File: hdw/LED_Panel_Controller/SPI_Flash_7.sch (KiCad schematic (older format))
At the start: 14 parts, among them U3101 74LVC1G97, U3102 SST25VF080B-50-4I-S2AF

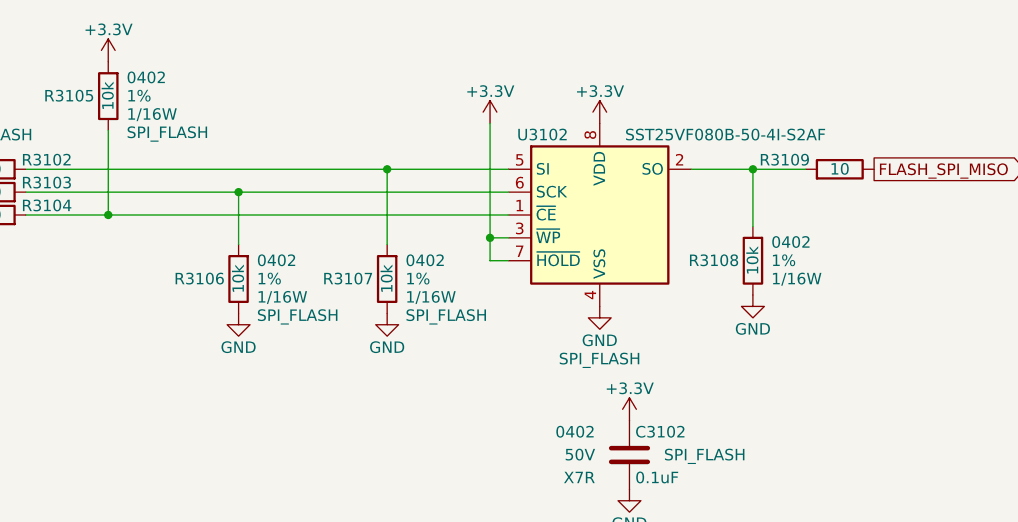
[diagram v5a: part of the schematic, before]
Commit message: fixed SPI flash pull resistors, more PCB placement
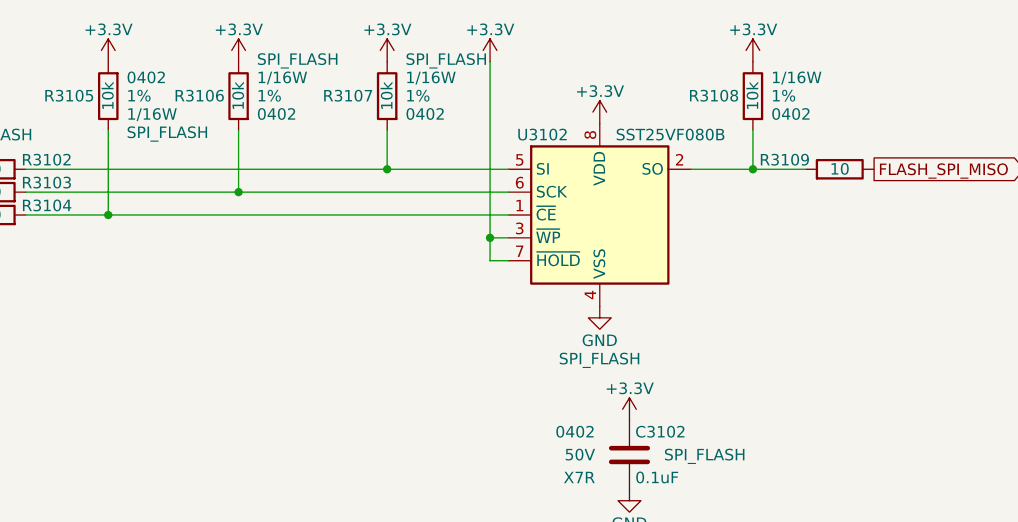
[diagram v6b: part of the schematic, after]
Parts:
- U3102: value SST25VF080B-50-4I-S2AF -> SST25VF080B
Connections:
- net +3V3: now also R3106.2, R3107.2, R3108.2
- net GND: no longer R3106.2, R3107.2, R3108.2
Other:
- moved on the sheet: R3106, R3107, R3108
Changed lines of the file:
@@
 L Custom_Library:R_Custom R3108
 U 1 1 60786265
-P 6750 3850
-F 0 "R3108" H 6690 3850 50  0000 R CNN
-F 1 "10k" V 6750 3850 50  0000 C CNN
-F 2 "Resistors_SMD:R_0402" H 6750 3850 50  0001 C CNN
-F 3 "" H 6750 3850 50  0001 C CNN
-F 4 "0402" H 6830 3930 50  0000 L CNN "display_footprint"
-F 5 "1%" H 6830 3850 50  0000 L CNN "Tolerance"
-F 6 "1/16W" H 6830 3770 50  0000 L CNN "Wattage"
-F 7 "RMCF0402FT10K0CT-ND" H 7050 4250 60  0001 C CNN "Digi-Key PN"
-	1    6750 3850
-	1    0    0    -1
-$EndComp
-$Comp
-L power:GND #PWR03108
-U 1 1 6078626D
-P 5150 4080
-F 0 "#PWR03108" H 5150 3830 50  0001 C CNN
-F 1 "GND" H 5150 3930 50  0000 C CNN
-F 2 "" H 5150 4080 50  0001 C CNN
-F 3 "" H 5150 4080 50  0001 C CNN
-	1    5150 4080
-	1    0    0    -1
-$EndComp
-$Comp
-L power:GND #PWR03114
-U 1 1 60786277
-P 6750 4000
-F 0 "#PWR03114" H 6750 3750 50  0001 C CNN
-F 1 "GND" H 6750 3850 50  0000 C CNN
-F 2 "" H 6750 4000 50  0001 C CNN
-F 3 "" H 6750 4000 50  0001 C CNN
-	1    6750 4000
-	1    0    0    -1
+P 6750 3130
+F 0 "R3108" H 6690 3130 50  0000 R CNN
+F 1 "10k" V 6750 3130 50  0000 C CNN
+F 2 "Resistors_SMD:R_0402" H 6750 3130 50  0001 C CNN
+F 3 "" H 6750 3130 50  0001 C CNN
+F 4 "0402" H 6830 3210 50  0000 L CNN "display_footprint"
+F 5 "1%" H 6830 3130 50  0000 L CNN "Tolerance"
+F 6 "1/16W" H 6830 3050 50  0000 L CNN "Wattage"
+F 7 "RMCF0402FT10K0CT-ND" H 7050 3530 60  0001 C CNN "Digi-Key PN"
+	1    6750 3130
+	1    0    0    1
 $EndComp
 $Comp
@@
 $EndComp
 Wire Wire Line
-	5150 3450 5150 3780
-Connection ~ 5150 3450
-Wire Wire Line
-	5150 3450 5680 3450
-Wire Wire Line
 	3930 3280 3930 3650
 Wire Wire Line
 	3930 3650 5680 3650
 Connection ~ 3930 3650
-Wire Wire Line
-	6980 3450 6750 3450
-Wire Wire Line
-	6750 3700 6750 3450
-Connection ~ 6750 3450
-Wire Wire Line
-	6750 3450 6480 3450
 Text GLabel 7280 3450 2    50   Output ~ 0
 FLASH_SPI_MISO
@@
 P 6080 3650
 F 0 "U3102" H 5830 4000 50  0000 C CNN
-F 1 "SST25VF080B-50-4I-S2AF" H 6630 4000 50  0000 C CNN
+F 1 "SST25VF080B" H 6630 4000 50  0000 R CNN
 F 2 "Package_SO:SOIC-8_5.275x5.275mm_P1.27mm" H 6080 2950 50  0001 C CNN
 F 3 "http://ww1.microchip.com/downloads/en/DeviceDoc/20005045C.pdf" H 6030 4200 50  0001 C CNN
@@
 L power:+3.3V #PWR03109
 U 1 1 6078630E
-P 5600 3250
-F 0 "#PWR03109" H 5600 3100 50  0001 C CNN
-F 1 "+3.3V" H 5600 3390 50  0000 C CNN
-F 2 "" H 5600 3250 50  0001 C CNN
-F 3 "" H 5600 3250 50  0001 C CNN
-	1    5600 3250
+P 5600 2980
+F 0 "#PWR03109" H 5600 2830 50  0001 C CNN
+F 1 "+3.3V" H 5600 3120 50  0000 C CNN
+F 2 "" H 5600 2980 50  0001 C CNN
+F 3 "" H 5600 2980 50  0001 C CNN
+	1    5600 2980
 	1    0    0    -1
 $EndComp
@@
 	5680 3750 5600 3750
 Wire Wire Line
-	5600 3750 5600 3250
+	5600 3750 5600 2980
 Wire Wire Line
 	5680 3850 5600 3850
@@
 	5600 3850 5600 3750
 Connection ~ 5600 3750
-Wire Wire Line
-	3570 3550 4500 3550
 $Comp
 L Custom_Library:R_Custom R3106
 U 1 1 60786315
-P 4500 3930
-F 0 "R3106" H 4440 3930 50  0000 R CNN
-F 1 "10k" V 4500 3930 50  0000 C CNN
-F 2 "Resistors_SMD:R_0402" H 4500 3930 50  0001 C CNN
-F 3 "" H 4500 3930 50  0001 C CNN
-F 4 "0402" H 4580 4010 50  0000 L CNN "display_footprint"
-F 5 "1%" H 4580 3930 50  0000 L CNN "Tolerance"
-F 6 "1/16W" H 4580 3850 50  0000 L CNN "Wattage"
-F 7 "RMCF0402FT10K0CT-ND" H 4800 4330 60  0001 C CNN "Digi-Key PN"
-F 8 "SPI_FLASH" H 4580 3770 50  0000 L CNN "Configuration"
-	1    4500 3930
-	1    0    0    -1
-$EndComp
-$Comp
-L power:GND #PWR03107
-U 1 1 6078631A
-P 4500 4080
-F 0 "#PWR03107" H 4500 3830 50  0001 C CNN
-F 1 "GND" H 4500 3930 50  0000 C CNN
-F 2 "" H 4500 4080 50  0001 C CNN
-F 3 "" H 4500 4080 50  0001 C CNN
-	1    4500 4080
-	1    0    0    -1
-$EndComp
-Wire Wire Line
-	3570 3450 5150 3450
-Wire Wire Line
-	4500 3550 4500 3780
-Connection ~ 4500 3550
-Wire Wire Line
-	4500 3550 5680 3550
+P 4500 3130
+F 0 "R3106" H 4440 3130 50  0000 R CNN
+F 1 "10k" V 4500 3130 50  0000 C CNN
+F 2 "Resistors_SMD:R_0402" H 4500 3130 50  0001 C CNN
+F 3 "" H 4500 3130 50  0001 C CNN
+F 4 "0402" H 4580 3210 50  0000 L CNN "display_footprint"
+F 5 "1%" H 4580 3130 50  0000 L CNN "Tolerance"
+F 6 "1/16W" H 4580 3050 50  0000 L CNN "Wattage"
+F 7 "RMCF0402FT10K0CT-ND" H 4800 3530 60  0001 C CNN "Digi-Key PN"
+F 8 "SPI_FLASH" H 4580 2970 50  0000 L CNN "Configuration"
+	1    4500 3130
+	1    0    0    1
+$EndComp
 $Comp
 L Custom_Library:R_Custom R3103
@@
 L Custom_Library:R_Custom R3107
 U 1 1 60786357
-P 5150 3930
-F 0 "R3107" H 5090 3930 50  0000 R CNN
-F 1 "10k" V 5150 3930 50  0000 C CNN
-F 2 "Resistors_SMD:R_0402" H 5150 3930 50  0001 C CNN
-F 3 "" H 5150 3930 50  0001 C CNN
-F 4 "0402" H 5230 4010 50  0000 L CNN "display_footprint"
-F 5 "1%" H 5230 3930 50  0000 L CNN "Tolerance"
-F 6 "1/16W" H 5230 3850 50  0000 L CNN "Wattage"
-F 7 "RMCF0402FT10K0CT-ND" H 5450 4330 60  0001 C CNN "Digi-Key PN"
-F 8 "SPI_FLASH" H 5230 3770 50  0000 L CNN "Configuration"
-	1    5150 3930
-	1    0    0    -1
+P 5150 3130
+F 0 "R3107" H 5090 3130 50  0000 R CNN
+F 1 "10k" V 5150 3130 50  0000 C CNN
+F 2 "Resistors_SMD:R_0402" H 5150 3130 50  0001 C CNN
+F 3 "" H 5150 3130 50  0001 C CNN
+F 4 "0402" H 5230 3210 50  0000 L CNN "display_footprint"
+F 5 "1%" H 5230 3130 50  0000 L CNN "Tolerance"
+F 6 "1/16W" H 5230 3050 50  0000 L CNN "Wattage"
+F 7 "RMCF0402FT10K0CT-ND" H 5450 3530 60  0001 C CNN "Digi-Key PN"
+F 8 "SPI_FLASH" H 5230 2970 50  0000 L CNN "Configuration"
+	1    5150 3130
+	1    0    0    1
 $EndComp
 $Comp
@@
 	1    0    0    -1
 $EndComp
+Wire Wire Line
+	3570 3450 5150 3450
+Wire Wire Line
+	3570 3550 4500 3550
+$Comp
+L power:+3.3V #PWR0124
+U 1 1 606A1000
+P 5150 2980
+F 0 "#PWR0124" H 5150 2830 50  0001 C CNN
+F 1 "+3.3V" H 5150 3120 50  0000 C CNN
+F 2 "" H 5150 2980 50  0001 C CNN
+F 3 "" H 5150 2980 50  0001 C CNN
+	1    5150 2980
+	1    0    0    -1
+$EndComp
+$Comp
+L power:+3.3V #PWR0125
+U 1 1 606A13DE
+P 4500 2980
+F 0 "#PWR0125" H 4500 2830 50  0001 C CNN
+F 1 "+3.3V" H 4500 3120 50  0000 C CNN
+F 2 "" H 4500 2980 50  0001 C CNN
+F 3 "" H 4500 2980 50  0001 C CNN
+	1    4500 2980
+	1    0    0    -1
+$EndComp
+Wire Wire Line
+	4500 3280 4500 3550
+Connection ~ 4500 3550
+Wire Wire Line
+	4500 3550 5680 3550
+Wire Wire Line
+	5150 3280 5150 3450
+Connection ~ 5150 3450
+Wire Wire Line
+	5150 3450 5680 3450
+Wire Wire Line
+	6480 3450 6750 3450
+$Comp
+L power:+3.3V #PWR0126
+U 1 1 606A26C8
+P 6750 2980
+F 0 "#PWR0126" H 6750 2830 50  0001 C CNN
+F 1 "+3.3V" H 6750 3120 50  0000 C CNN
+F 2 "" H 6750 2980 50  0001 C CNN
+F 3 "" H 6750 2980 50  0001 C CNN
+	1    6750 2980
+	1    0    0    -1
+$EndComp
+Wire Wire Line
+	6750 3280 6750 3450
+Connection ~ 6750 3450
+Wire Wire Line
+	6750 3450 6980 3450
 $EndSCHEMATC

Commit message: added BOMs, some consolidation
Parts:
- C3101, C3102: Digi-Key PN 490-10701-1-ND -> 490-10698-1-ND
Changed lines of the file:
@@
 F 5 "50V" H 1860 6900 50  0000 R CNN "Voltage"
 F 6 "X7R" H 1860 6800 50  0000 R CNN "Dielectric"
-F 7 "490-10701-1-ND" H 2435 7400 60  0001 C CNN "Digi-Key PN"
+F 7 "490-10698-1-ND" H 2435 7400 60  0001 C CNN "Digi-Key PN"
 F 8 "SPI_FLASH" H 2340 6900 50  0000 C CNN "Configuration"
 	1    2010 6900
@@
 F 5 "50V" H 6060 4700 50  0000 R CNN "Voltage"
 F 6 "X7R" H 6060 4600 50  0000 R CNN "Dielectric"
-F 7 "490-10701-1-ND" H 6635 5200 60  0001 C CNN "Digi-Key PN"
+F 7 "490-10698-1-ND" H 6635 5200 60  0001 C CNN "Digi-Key PN"
 F 8 "SPI_FLASH" H 6540 4700 50  0000 C CNN "Configuration"
 	1    6210 4700
